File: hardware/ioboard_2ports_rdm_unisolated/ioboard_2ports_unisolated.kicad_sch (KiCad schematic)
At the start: 31 parts, among them J1 Conn_02x06_Odd_Even, J12 Conn_01x03, J2 XLR3, J3 XLR3, J4 8P8C, J5 8P8C, J6 Conn_01x03, J8 XLR3, J9 XLR3, U1 M24C64-RMN6TP, U2 SP3485EN, U3 AMS1117-3.3, U4 SP3485EN

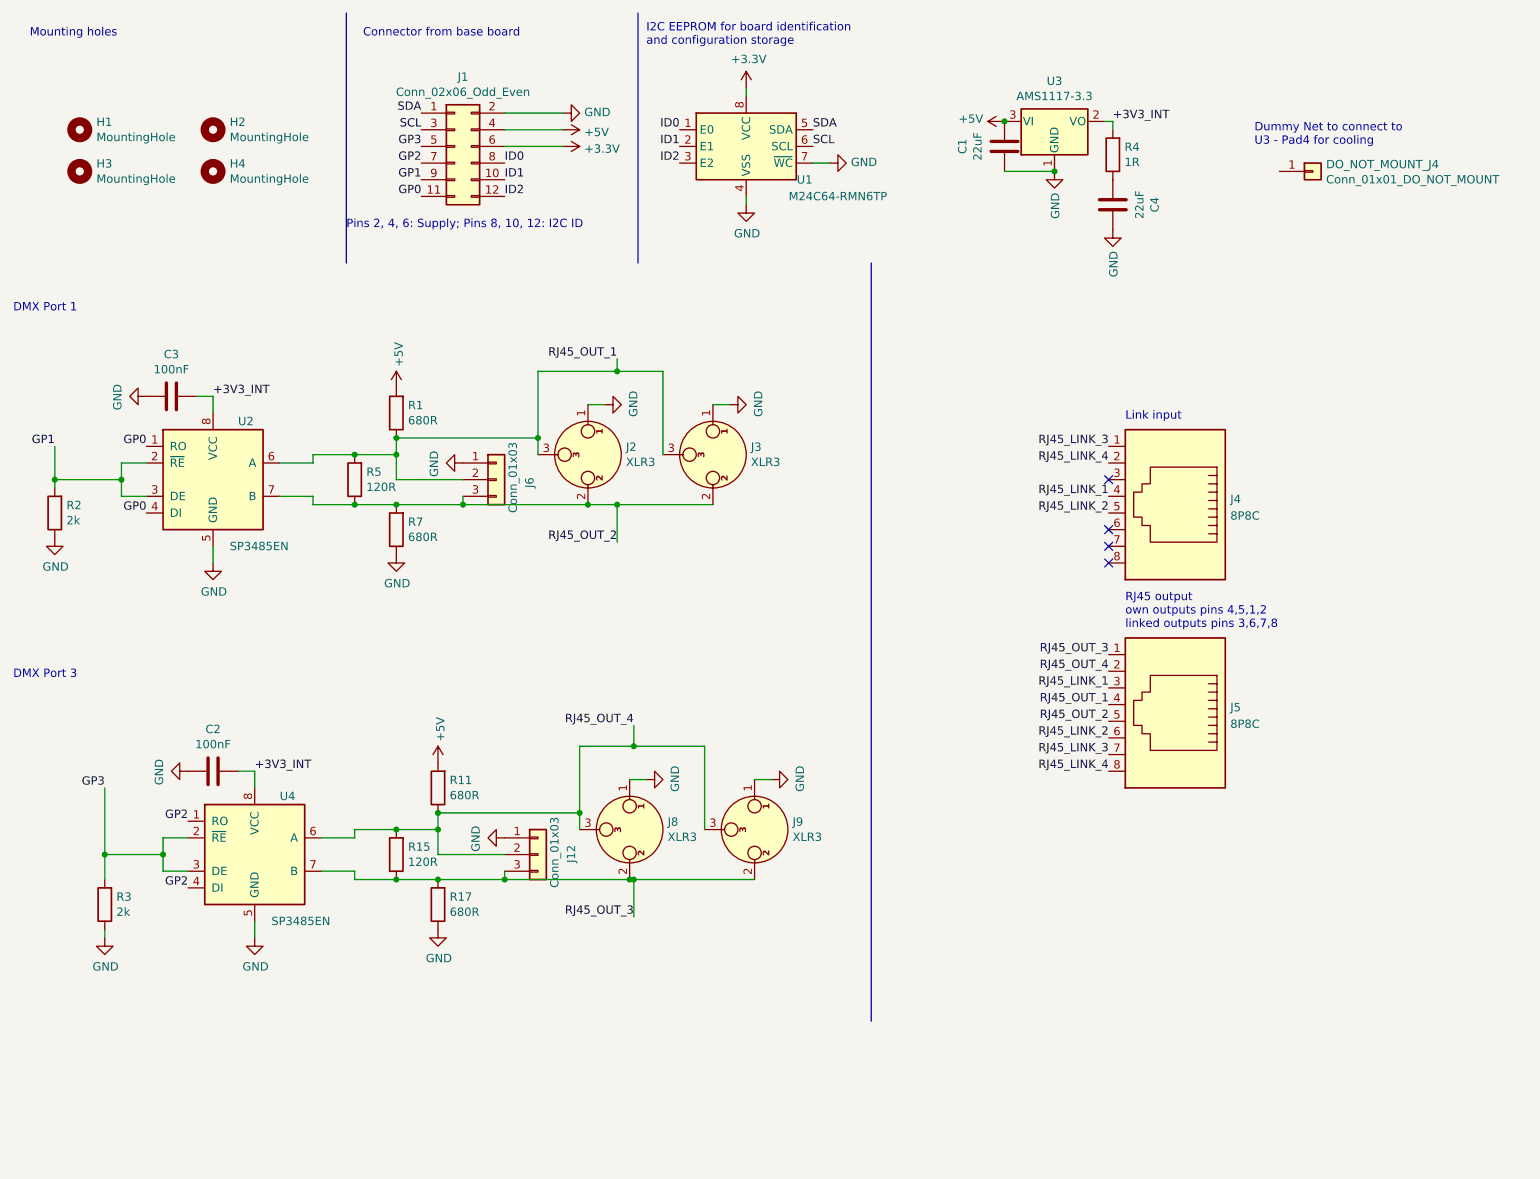
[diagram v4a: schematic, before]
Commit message: Update ioboards to KiCad 8, add OpenHardware logo
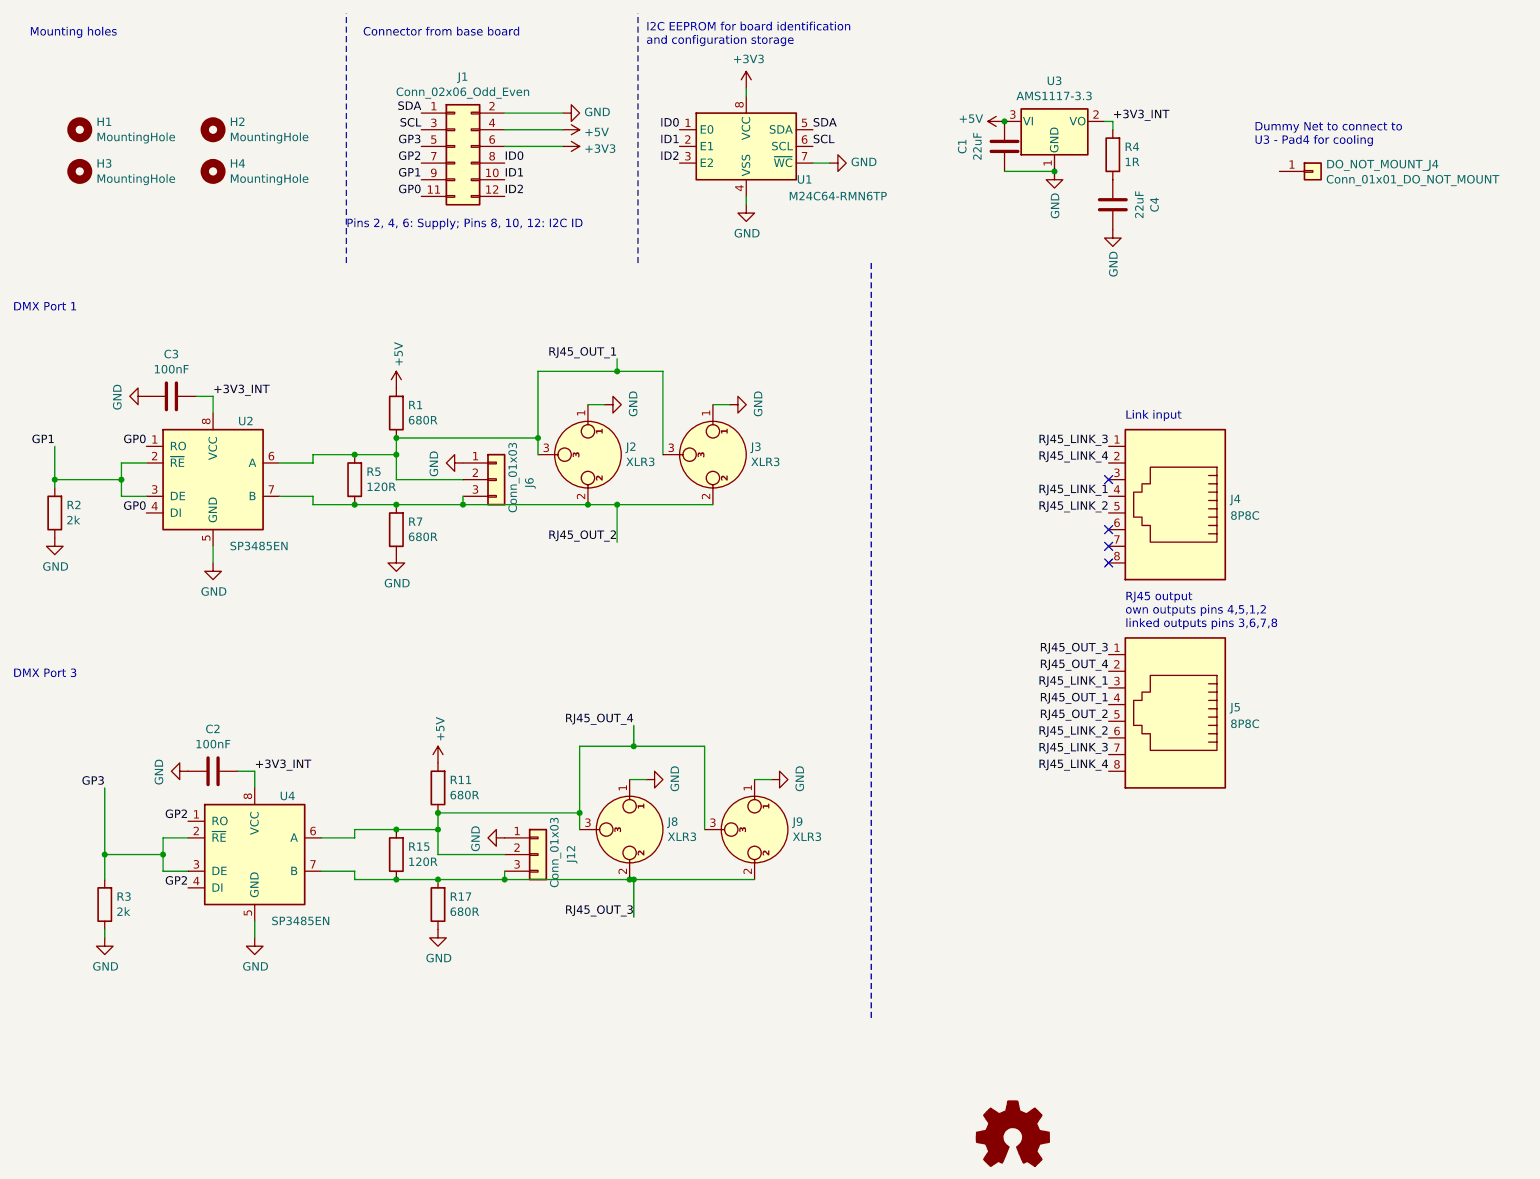
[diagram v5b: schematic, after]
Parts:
- added SYM1: Logo_Open_Hardware_Small, Symbol:OSHW-Logo2_14.6x12mm_SilkScreen, symbol Graphic:Logo_Open_Hardware_Small
